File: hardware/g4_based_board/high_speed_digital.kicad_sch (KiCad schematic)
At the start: 4 parts, among them J6 Conn_01x04, J7 Conn_01x05_Socket

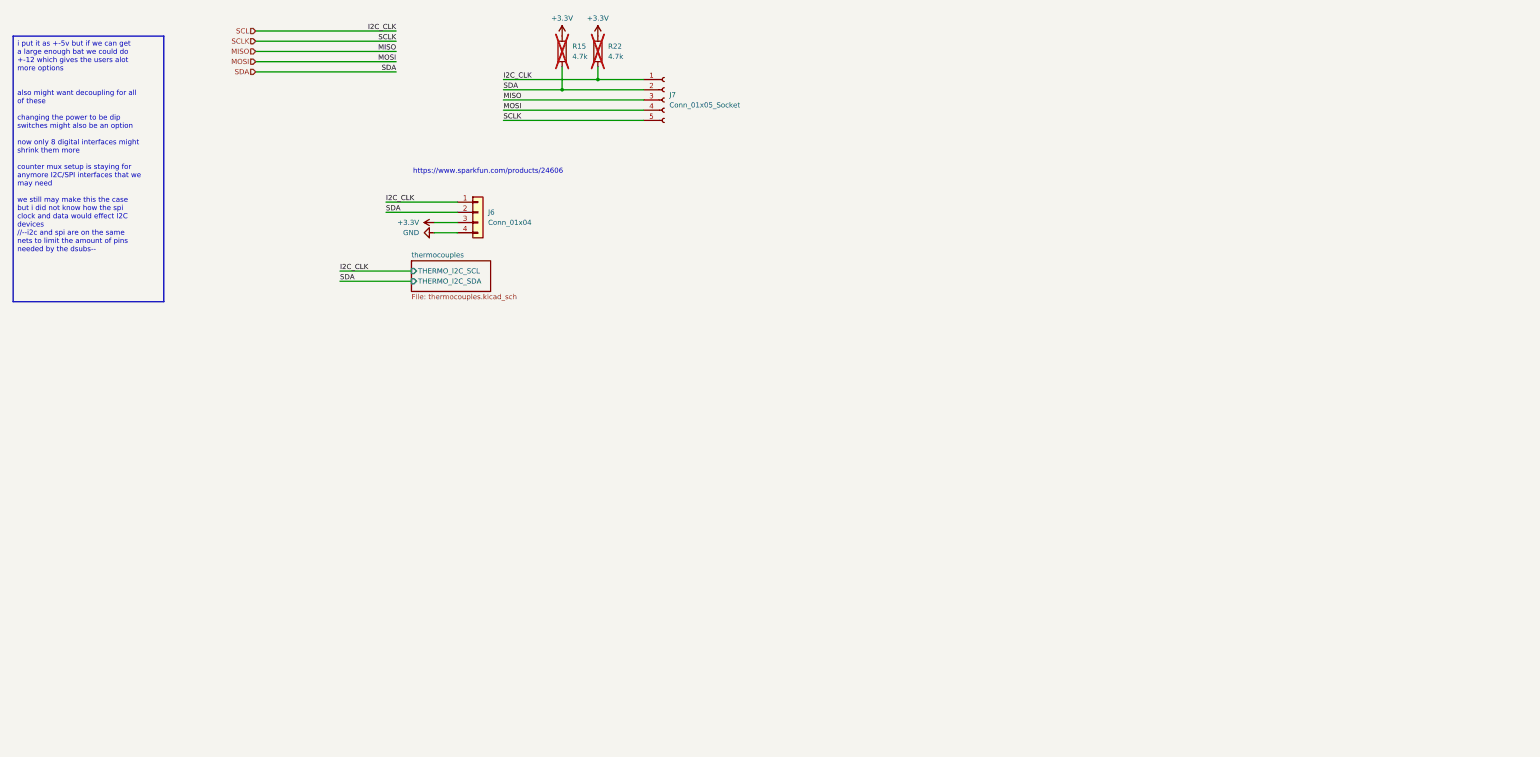
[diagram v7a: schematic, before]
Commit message: added thermo sensor in here, added BME680, all off board i2c lines now have a bus buffer
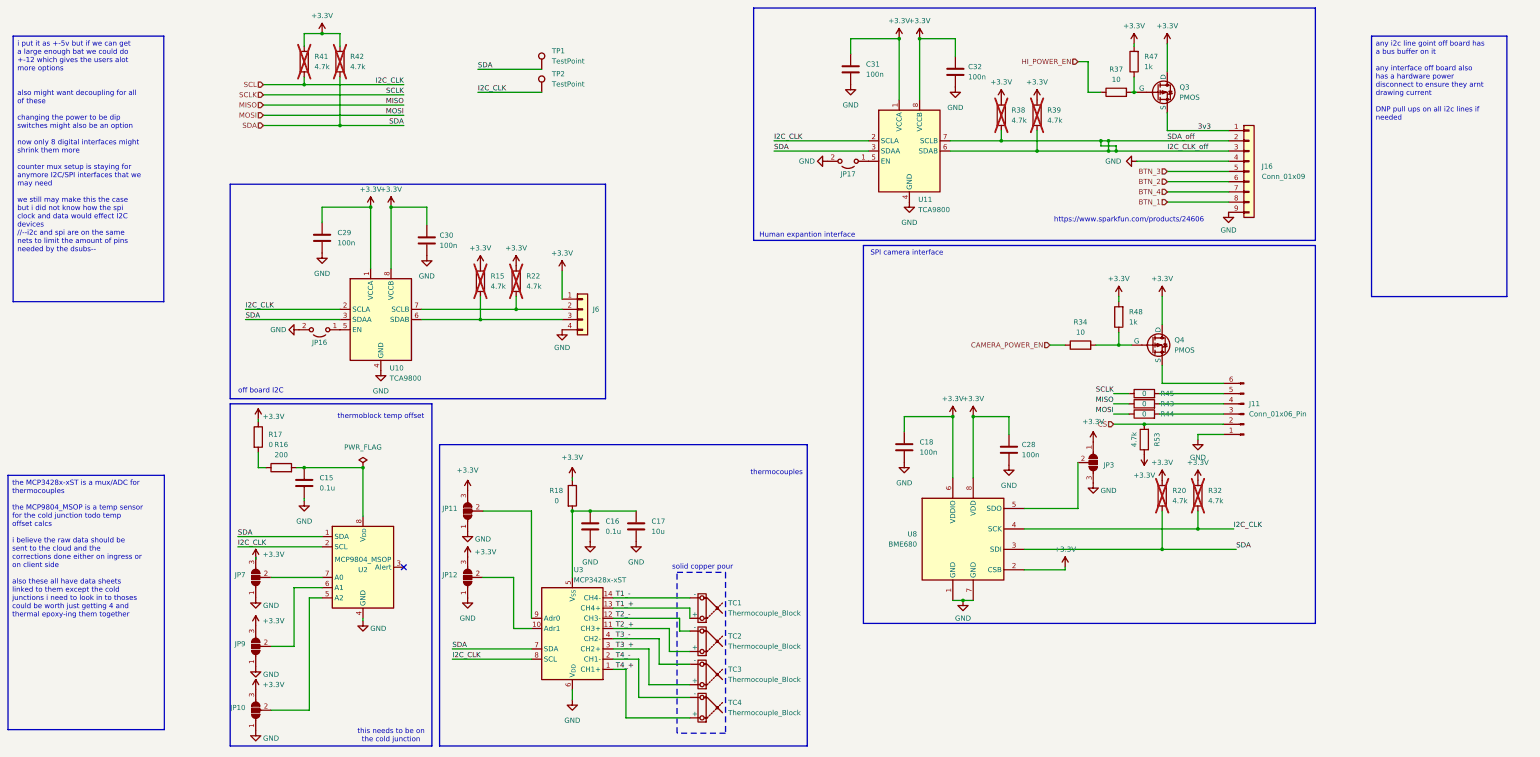
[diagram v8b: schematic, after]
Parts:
- removed J7: Conn_01x05_Socket, Connector_PinHeader_2.54mm:PinHeader_1x05_P2.54mm_Vertical, symbol Connector:Conn_01x05_Socket
- added C15, C16: 0.1u, Capacitor_SMD:C_0603_1608Metric_Pad1.08x0.95mm_HandSolder, symbol Device:C
- added C17: 10u, Capacitor_SMD:C_0603_1608Metric_Pad1.08x0.95mm_HandSolder, symbol Device:C
- added C18, C28, C29, C30, C31, C32: 100n, Capacitor_SMD:C_0603_1608Metric_Pad1.08x0.95mm_HandSolder, symbol Device:C
- added J11: Conn_01x06_Pin, Connector_JST:JST_XH_B6B-XH-A_1x06_P2.50mm_Vertical, symbol Connector:Conn_01x06_Pin
- added J16: Conn_01x09, Connector_JST:JST_XH_B9B-XH-A_1x09_P2.50mm_Vertical, symbol Connector_Generic:Conn_01x09
- added JP10, JP11, JP12, JP3, JP7, JP9: ~, Jumper:SolderJumper-3_P1.3mm_Open_RoundedPad1.0x1.5mm, symbol Jumper:SolderJumper_3_Open
- added JP16, JP17: Jumper_2_Open, Jumper:SolderJumper-2_P1.3mm_Open_TrianglePad1.0x1.5mm, symbol Jumper:Jumper_2_Open
- added Q3, Q4: PMOS, Package_TO_SOT_SMD:SOT-23-3, symbol Simulation_SPICE:PMOS
- added R16: 200, Resistor_SMD:R_0603_1608Metric_Pad0.98x0.95mm_HandSolder, symbol Device:R
- added R17, R18, R43, R44, R45: 0, Resistor_SMD:R_0603_1608Metric_Pad0.98x0.95mm_HandSolder, symbol Device:R
- added R20, R32, R38, R39, R41, R42, R53: 4.7k, Resistor_SMD:R_0603_1608Metric_Pad0.98x0.95mm_HandSolder, symbol Device:R
- added R34, R37: 10, Resistor_SMD:R_0603_1608Metric_Pad0.98x0.95mm_HandSolder, symbol Device:R
- added R47, R48: 1k, Resistor_SMD:R_0603_1608Metric_Pad0.98x0.95mm_HandSolder, symbol Device:R
- added TC1, TC2, TC3, TC4: Thermocouple_Block, TerminalBlock:TerminalBlock_Altech_AK300-2_P5.00mm, symbol Device:Thermocouple_Block
- added TP1, TP2: TestPoint, TestPoint:TestPoint_Keystone_5015_Micro-Minature, symbol Connector:TestPoint
- added U10, U11: TCA9800, Package_SO:VSSOP-8_3.0x3.0mm_P0.65mm, symbol Interface:TCA9800
- added U2: MCP9804_MSOP, Package_SO:MSOP-8_3x3mm_P0.65mm, symbol Sensor_Temperature:MCP9804_MSOP
- added U3: MCP3428x-xST, Package_SO:TSSOP-14_4.4x5mm_P0.65mm, symbol Analog_ADC:MCP3428x-xST
- added U8: BME680, Package_LGA:Bosch_LGA-8_3x3mm_P0.8mm_ClockwisePinNumbering, symbol Sensor:BME680
- J6: footprint Connector_Molex:Molex_KK-254_AE-6410-04A_1x04_P2.54mm_Vertical -> Connector_PinHeader_2.54mm:PinHeader_1x04_P2.54mm_Vertical
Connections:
- net +3.3V: now also J6.1 (Pin_1), C18.1, C28.1, C29.1, C30.1, C31.1, C32.1, JP10.3 (B), JP11.3 (B), JP12.3 (B), JP3.1 (A), JP7.3 (B), JP9.3 (B), Q3.1 (D), Q4.1 (D), R17.1, R18.1, R20.1, R32.1, R38.1, R39.1, R41.1, R42.1, R47.2, R48.2, R53.1, U10.1 (VCCA), U10.8 (VCCB), U11.1 (VCCA), U11.8 (VCCB), U8.2 (CSB), U8.6 (VDDIO), U8.8 (VDD); no longer J6.3 (Pin_3)
- net GND: now also C15.2, C16.2, C17.2, C18.2, C28.2, C29.2, C30.2, C31.2, C32.2, J11.1 (Pin_1), J16.4 (Pin_4), J16.9 (Pin_9), JP10.1 (A), JP11.1 (A), JP12.1 (A), JP16.2 (B), JP17.2 (B), JP3.3 (B), JP7.1 (A), JP9.1 (A), U10.4 (GND), U11.4 (GND), U2.4 (GND), U3.6 (V_{DD}), U8.1 (GND), U8.7 (GND)
- net MISO: now also R43.1
- net MOSI: now also R44.1
- net SCL: now also R32.2, R41.2, TP2.1, U10.2 (SCLA), U11.2 (SCLA), U2.2 (SCL), U3.8 (SCL), U8.4 (SCK); no longer J6.1 (Pin_1), R22.2
- net SCLK: now also R45.1
- net SDA: now also R20.2, R42.2, TP1.1, U10.3 (SDAA), U11.3 (SDAA), U2.1 (SDA), U3.7 (SDA), U8.3 (SDI); no longer J6.2 (Pin_2), R15.2
- new net: JP7.2 (C), U2.7 (A0)
- new net: JP3.2 (C), U8.5 (SDO)
- new net: JP17.1 (A), U11.5 (EN)
- new net: Q3.2 (G), R37.2, R47.1
- new net: J11.5 (Pin_5), R45.2
- new net: J11.4 (Pin_4), R43.2
- new net: Q4.2 (G), R34.2, R48.1
- new net: JP9.2 (C), U2.6 (A1)
- new net: JP12.2 (C), U3.10 (Adr1)
- new net: C16.1, C17.1, R18.2, U3.5 (V_{SS})
- new net: JP11.2 (C), U3.9 (Adr0)
- new net: J6.3 (Pin_3), R15.2, U10.6 (SDAB)
- new net: JP16.1 (A), U10.5 (EN)
- new net: J6.2 (Pin_2), R22.2, U10.7 (SCLB)
- new net: JP10.2 (C), U2.5 (A2)
- new net: C15.1, R16.2, U2.8 (V_{DD})
- new net: R16.1, R17.2
- new net: J11.3 (Pin_3), R44.2
- new net: J11.6 (Pin_6), Q4.3 (S)
- new net 3v3: J16.1 (Pin_1), Q3.3 (S)
- new net BTN_1: J16.8 (Pin_8)
- new net BTN_2: J16.6 (Pin_6)
- new net BTN_3: J16.5 (Pin_5)
- new net BTN_4: J16.7 (Pin_7)
- new net CAMERA_POWER_EN: R34.1
- new net CS: J11.2 (Pin_2), R53.2
- new net HI_POWER_EN: R37.1
- new net I2C_CLK_off: J16.2 (Pin_2), J16.3 (Pin_3), R38.2, R39.2, U11.6 (SDAB), U11.7 (SCLB)
- new net T1_+: TC1.1 (+), U3.13 (CH4+)
- new net T1_-: TC1.2 (-), U3.14 (CH4-)
- new net T2_+: TC2.1 (+), U3.11 (CH3+)
- new net T2_-: TC2.2 (-), U3.12 (CH3-)
- new net T3_+: TC3.1 (+), U3.3 (CH2+)
- new net T3_-: TC3.2 (-), U3.4 (CH2-)
- new net T4_+: TC4.1 (+), U3.1 (CH1+)
- new net T4_-: TC4.2 (-), U3.2 (CH1-)
- no-connect marks 0 -> 1
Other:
- removed sheet thermocouples
- note added: "Human expantion interface"
- note added: "SPI camera interface"
- note added: "off board I2C"
- note added: "solid copper pour"
- note added: "thermoblock temp offset"
- note added: "thermocouples"
- note added: "this needs to be on the cold junction"
